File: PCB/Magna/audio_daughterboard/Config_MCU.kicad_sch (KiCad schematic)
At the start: 11 parts, among them J1401 Conn_01x03_Pin, J1402 Conn_ARM_SWD_TagConnect_TC2030, J1403 Conn_01x02_Pin, J1404 Conn_01x02_Pin, U1401 STM32F030C8Tx

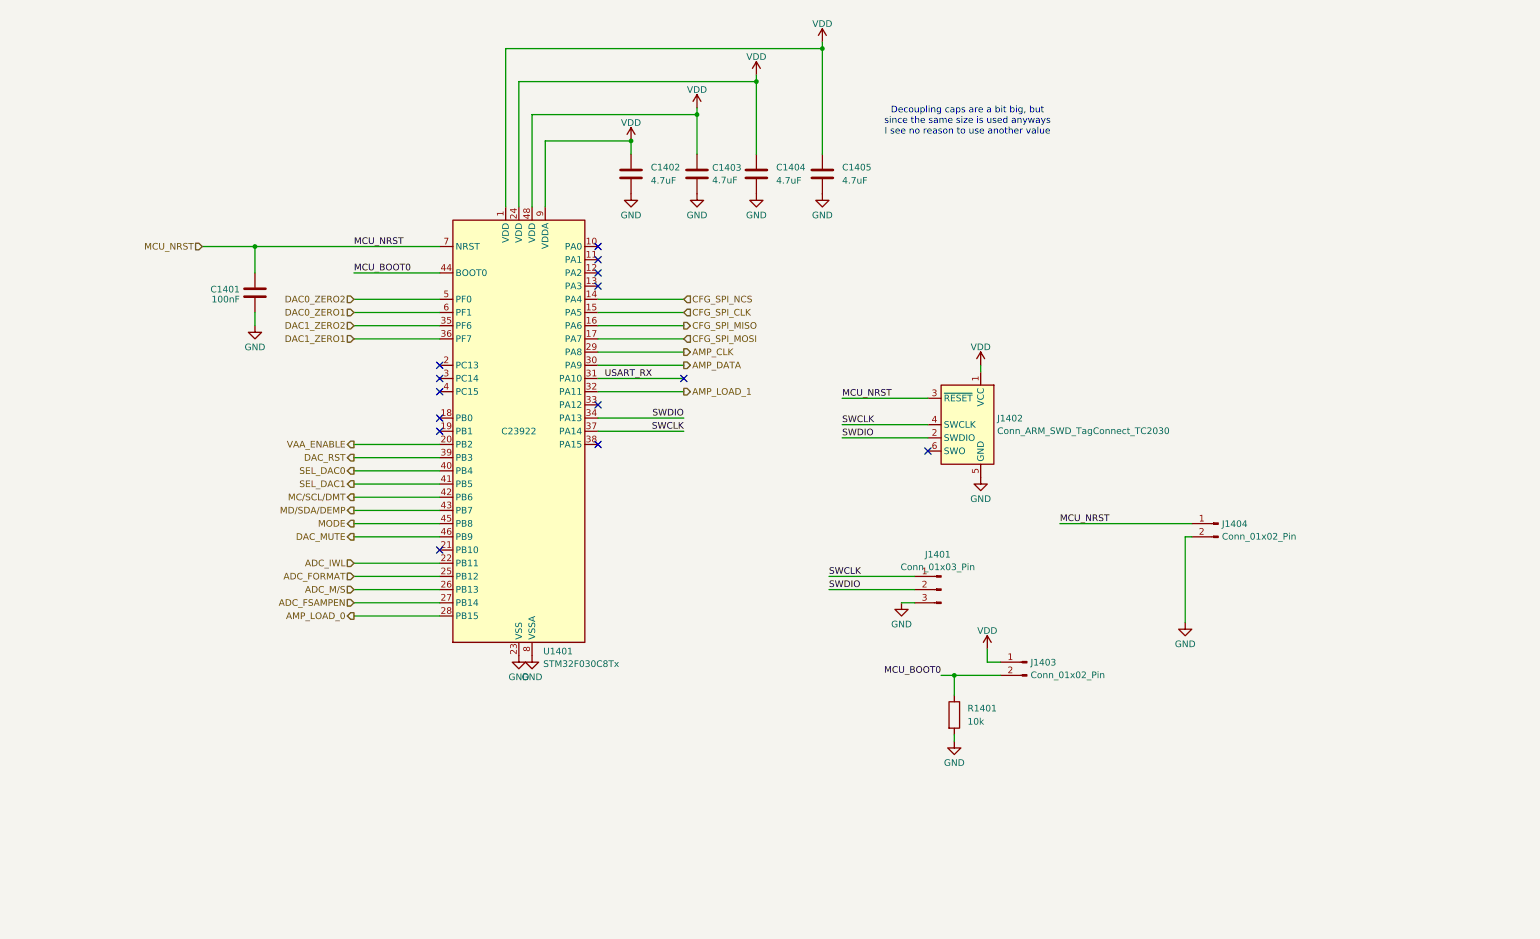
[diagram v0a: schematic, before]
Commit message: Do most of the component placement for audio board
Just a general layout, things will probably change
as the routing begins.
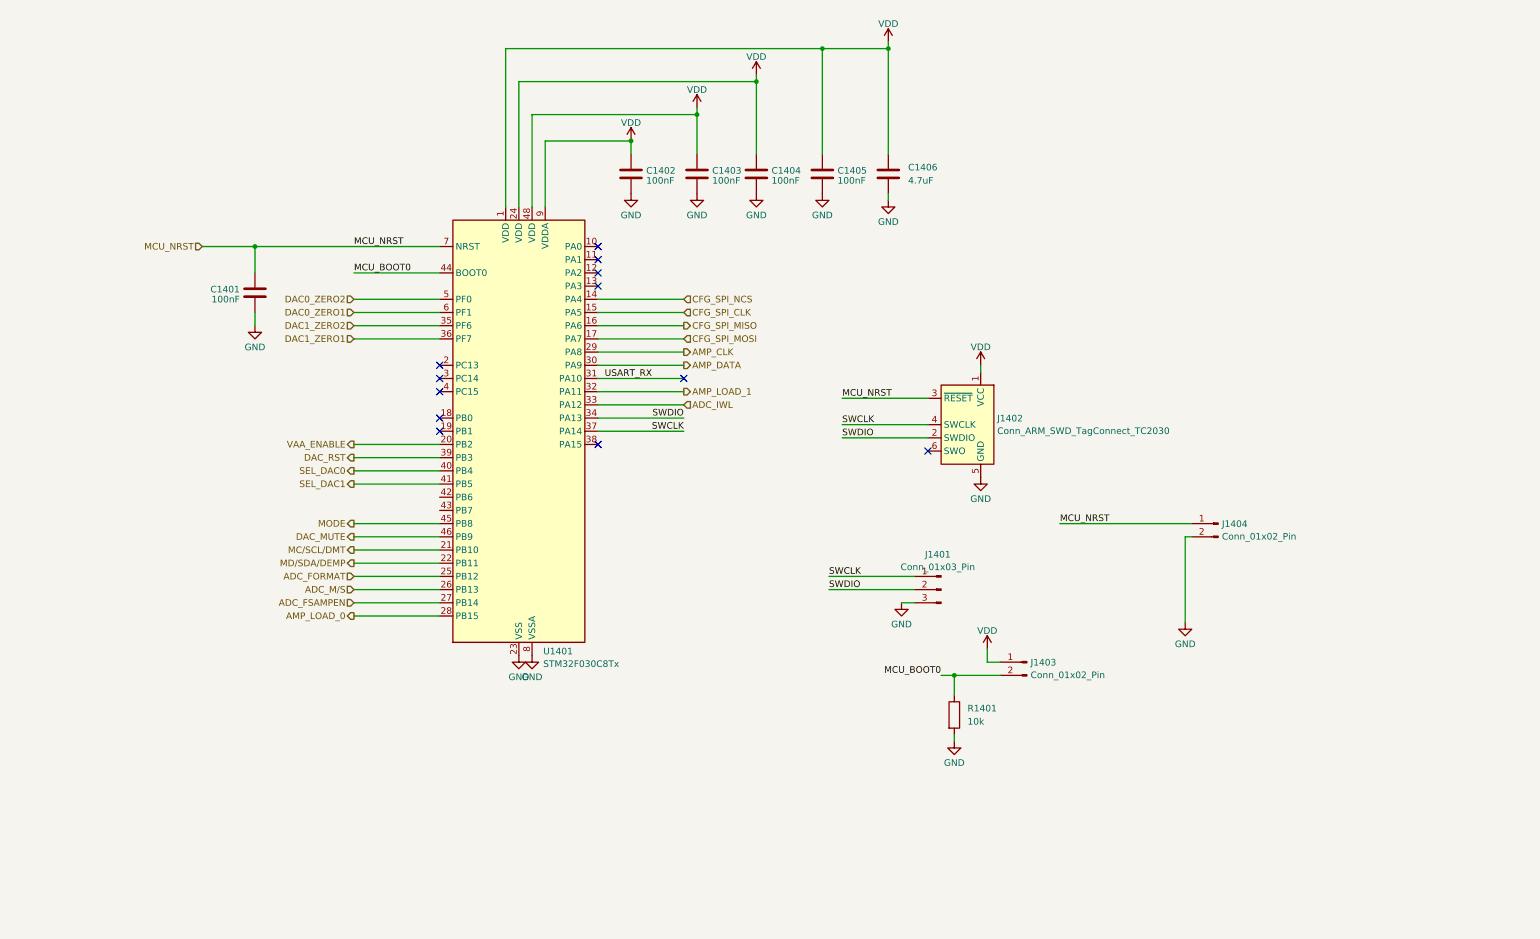
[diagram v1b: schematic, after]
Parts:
- added C1405: 100nF, Capacitor_SMD:C_0603_1608Metric, symbol Device:C
- C1401: footprint Capacitor_SMD:C_0805_2012Metric_Pad1.18x1.45mm_HandSolder -> Capacitor_SMD:C_0603_1608Metric; LCSC C49678 -> C14663
- C1402, C1403, C1404: value 4.7uF -> 100nF; footprint Capacitor_SMD:C_0805_2012Metric_Pad1.18x1.45mm_HandSolder -> Capacitor_SMD:C_0603_1608Metric; LCSC C1779 -> C14663
- C1406: renamed from C1405; footprint Capacitor_SMD:C_0805_2012Metric_Pad1.18x1.45mm_HandSolder -> Capacitor_SMD:C_1206_3216Metric; LCSC C1779 -> C29823
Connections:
- net ADC_IWL: now also U1401.33 (PA12); no longer U1401.22 (PB11)
- net GND: now also C1405.2
- net MC/SCL/DMT: now also U1401.21 (PB10); no longer U1401.42 (PB6)
- net MD/SDA/DEMP: now also U1401.22 (PB11); no longer U1401.43 (PB7)
- net VDD: now also C1405.1
- no-connect marks 14 -> 12
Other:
- note removed: "Decoupling caps are a bit big, but since the same size is used anyways I see no reason to use another value"
- moved on the sheet: C1406

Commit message: Start layout and routing of Audio Daugherboard
Also a lot of small changes to everything that became apperant
when the audio daughterboard was designed. Such as the Headphone
PCB, which is now separate from the rest of the audio.
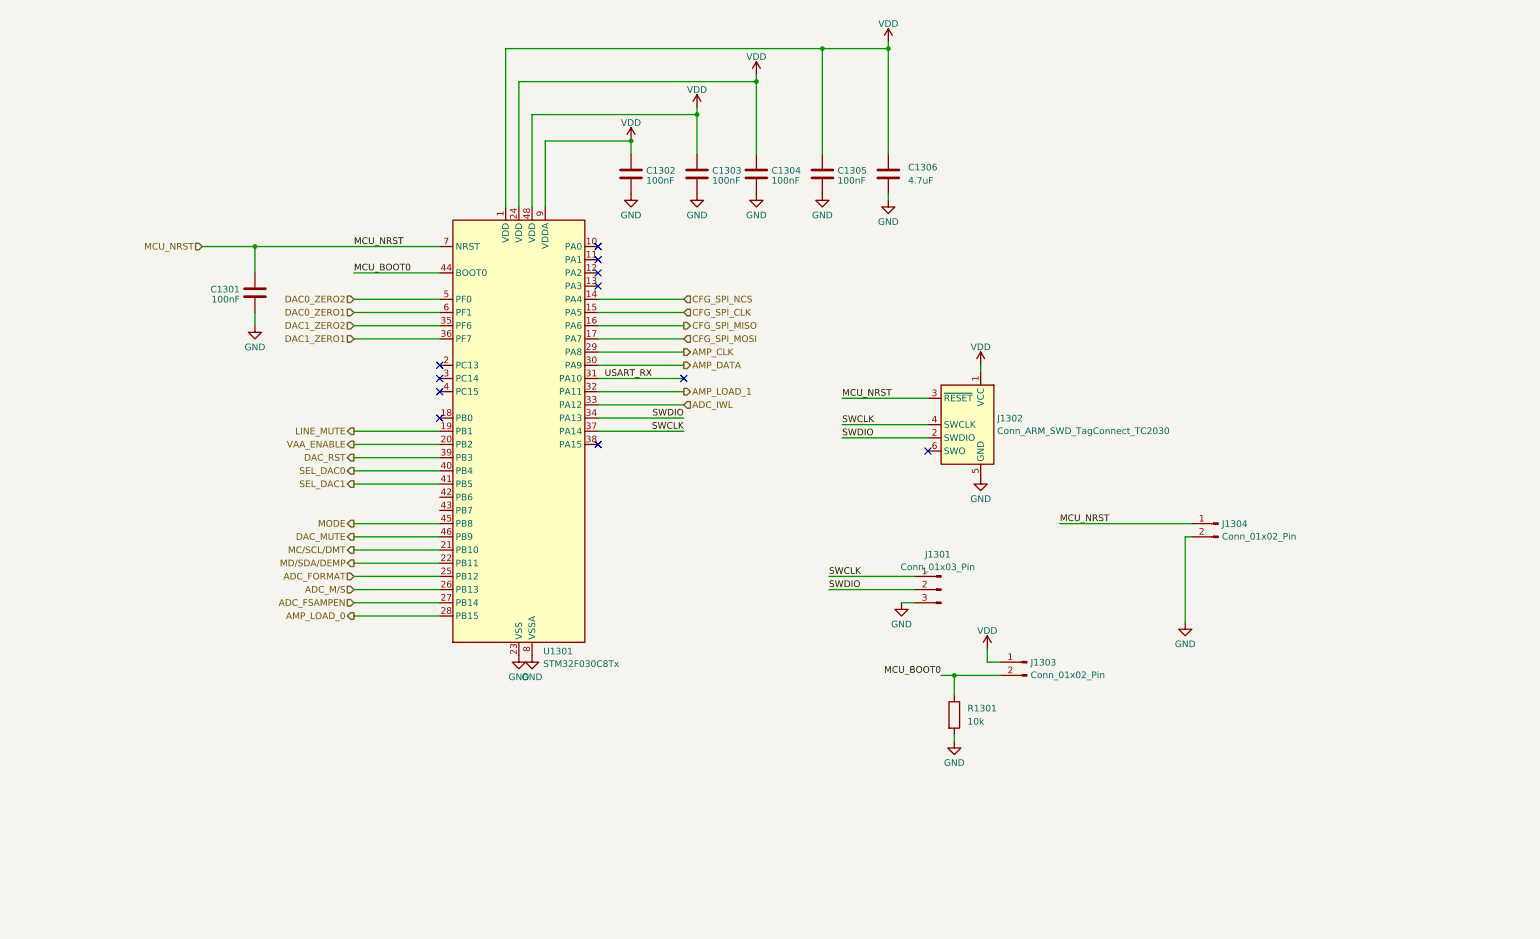
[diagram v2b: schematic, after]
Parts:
- renumbered C1401 to C1301, C1402 to C1302, C1403 to C1303, C1404 to C1304, C1405 to C1305, C1406 to C1306, J1401 to J1301, J1402 to J1302, J1403 to J1303, J1404 to J1304, R1401 to R1301, U1401 to U1301
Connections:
- net LINE_MUTE: now reaches U1301.19 (PB1)
- no-connect marks 12 -> 11

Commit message: Finished first round of routing for the Audio Daughterboard
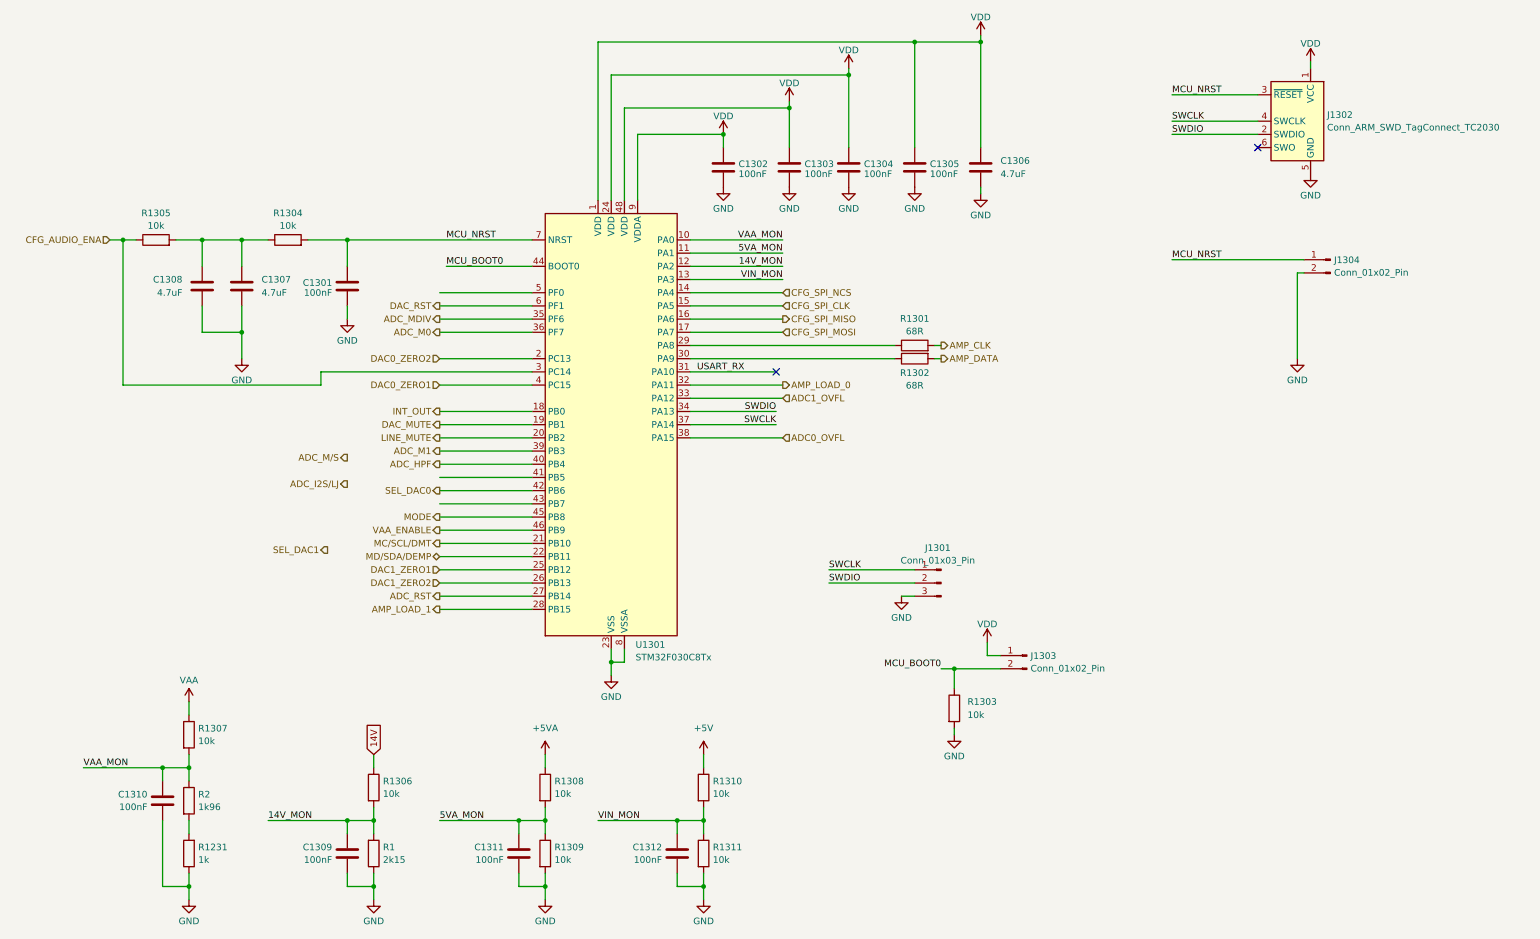
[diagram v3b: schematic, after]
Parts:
- added C1307, C1308: 4.7uF, Capacitor_SMD:C_1206_3216Metric, symbol Device:C
- added C1309, C1310, C1311, C1312: 100nF, Capacitor_SMD:C_0603_1608Metric, symbol Device:C
- added R1: 2k15, Resistor_SMD:R_0603_1608Metric, symbol Device:R
- added R1231: 1k, Resistor_SMD:R_0603_1608Metric, symbol Device:R
- added R1301, R1302: 68R, Resistor_SMD:R_0603_1608Metric, symbol Device:R
- added R1304, R1305, R1306, R1307, R1308, R1309, R1310, R1311: 10k, Resistor_SMD:R_0603_1608Metric, symbol Device:R
- added R2: 1k96, Resistor_SMD:R_0603_1608Metric, symbol Device:R
- R1303: renamed from R1301; now in the parts list
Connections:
- net ADC_FORMAT is gone; now on net DAC1_ZERO1: U1301.25 (PB12)
- net ADC_M/S: no longer U1301.26 (PB13)
- net AMP_CLK: now also R1301.2; no longer U1301.29 (PA8)
- net AMP_DATA: now also R1302.2; no longer U1301.30 (PA9)
- net AMP_LOAD_0: now also U1301.32 (PA11); no longer U1301.28 (PB15)
- net AMP_LOAD_1: now also U1301.28 (PB15); no longer U1301.32 (PA11)
- net DAC0_ZERO1: now also U1301.4 (PC15); no longer U1301.6 (PF1)
- net DAC0_ZERO2: now also U1301.2 (PC13); no longer U1301.5 (PF0)
- net DAC1_ZERO1: no longer U1301.36 (PF7)
- net DAC1_ZERO2: now also U1301.26 (PB13); no longer U1301.35 (PF6)
- net DAC_MUTE: now also U1301.19 (PB1); no longer U1301.46 (PB9)
- net DAC_RST: now also U1301.6 (PF1); no longer U1301.39 (PB3)
- net GND: now also C1307.2, C1308.2, C1309.2, C1310.2, C1311.2, C1312.2, R1.1, R1231.1, R1309.2, R1311.2
- net LINE_MUTE: now also U1301.20 (PB2); no longer U1301.19 (PB1)
- net MCU_NRST: now also R1304.2
- net SEL_DAC0: now also U1301.42 (PB6); no longer U1301.40 (PB4)
- net SEL_DAC1: no longer U1301.41 (PB5)
- net VAA_ENABLE: now also U1301.46 (PB9); no longer U1301.20 (PB2)
- net VAA_MON: now reaches U1301.10 (PA0)
- net VAA_MON: now also C1310.1, R1307.2, R2.1
- net 5VA_MON: now reaches U1301.11 (PA1)
- net 5VA_MON: now also C1311.1, R1308.2, R1309.1
- net 14V_MON: now reaches U1301.12 (PA2)
- net 14V_MON: now also C1309.1, R1.2, R1306.2
- net VIN_MON: now reaches U1301.13 (PA3)
- net VIN_MON: now also C1312.1, R1310.2, R1311.1
- net INT_OUT: now reaches U1301.18 (PB0)
- net CFG_AUDIO_ENA: now reaches U1301.3 (PC14)
- net CFG_AUDIO_ENA: now also R1305.1
- net ADC0_OVFL: now reaches U1301.38 (PA15)
- net ADC_FSAMPEN renamed ADC_RST
- net ADC_IWL renamed ADC1_OVFL
- new net: C1307.1, C1308.1, R1304.1, R1305.2
- new net: R1231.2, R2.2
- new net: R1301.1, U1301.29 (PA8)
- new net: R1302.1, U1301.30 (PA9)
- new net +5V: R1310.1
- new net +5VA: R1308.1
- new net 14V: R1306.1
- new net ADC_HPF: U1301.40 (PB4)
- new net ADC_M0: U1301.36 (PF7)
- new net ADC_M1: U1301.39 (PB3)
- new net ADC_MDIV: U1301.35 (PF6)
- new net VAA: R1307.1
- no-connect marks 11 -> 2
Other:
- moved on the sheet: C1301, C1302, C1303, C1304, C1305, C1306, J1301, J1302, J1303, J1304, R1303, U1301
